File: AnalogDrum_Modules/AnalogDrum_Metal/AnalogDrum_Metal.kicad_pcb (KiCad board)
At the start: 2 copper layers, 100.3 x 160 mm, 177 parts, among them J101 Conn_01x05_Male, Q201 2N3904, Q202 2N3904, Q203 2N3904, Q501 2N3906, Q502 2N3906, Q503 2N3906, Q504 2N3904, Q505 2N3904, Q506 2N3904, Q701 2N3904, Q702 2N3904, Q703 2N3904, SW601 SW_DPDT_x2, SW602 SW_DPDT_x2, U201 TL074, U202 LM358, U301 NE5532, U401 NE5532, U402 LM13700, U403 NE5532, U501 NE5532, U502 NE5532, U601 TL074, U701 TL074, U702 LM358

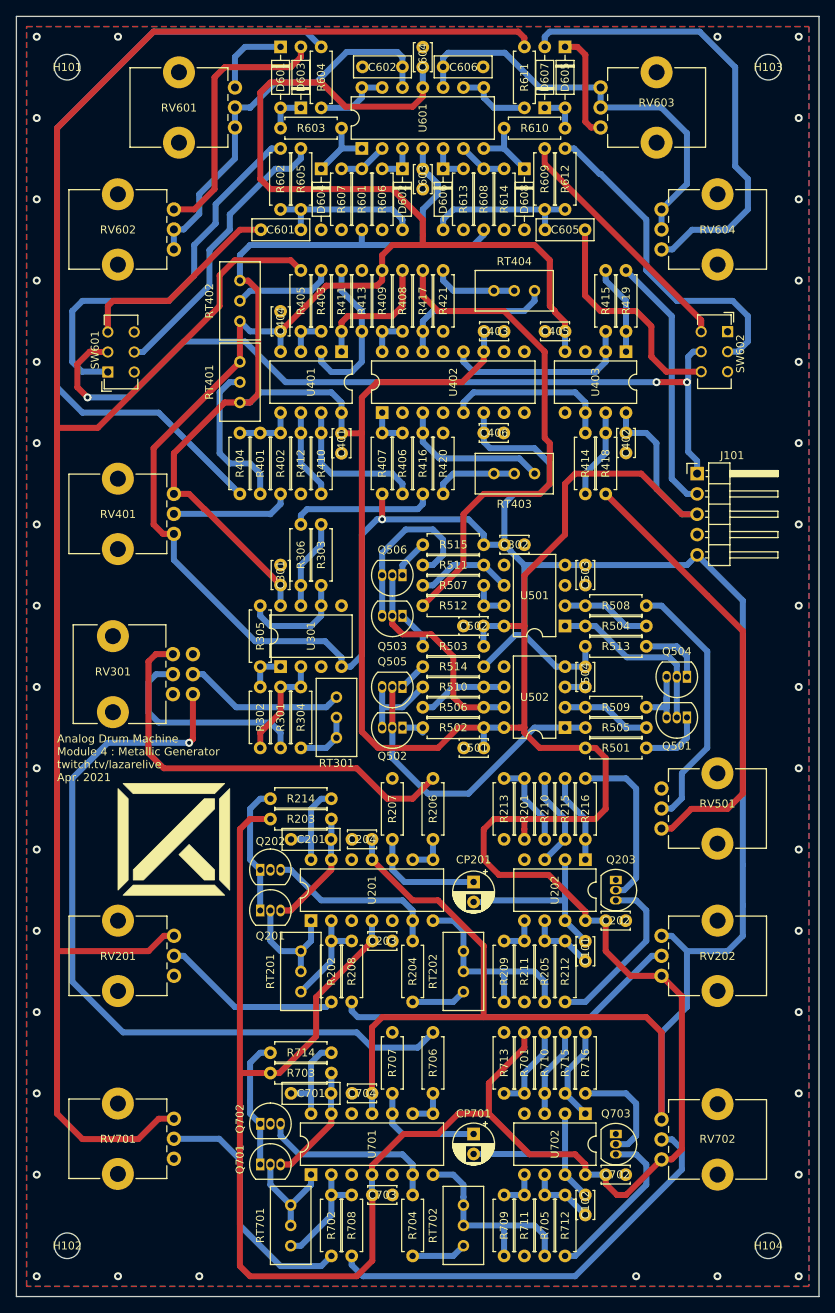
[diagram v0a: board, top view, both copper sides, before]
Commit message: Version 0.1.1
Corrections mineures :
- Vérification des potentiomètres
- Passage des connecteurs de carte e n JST
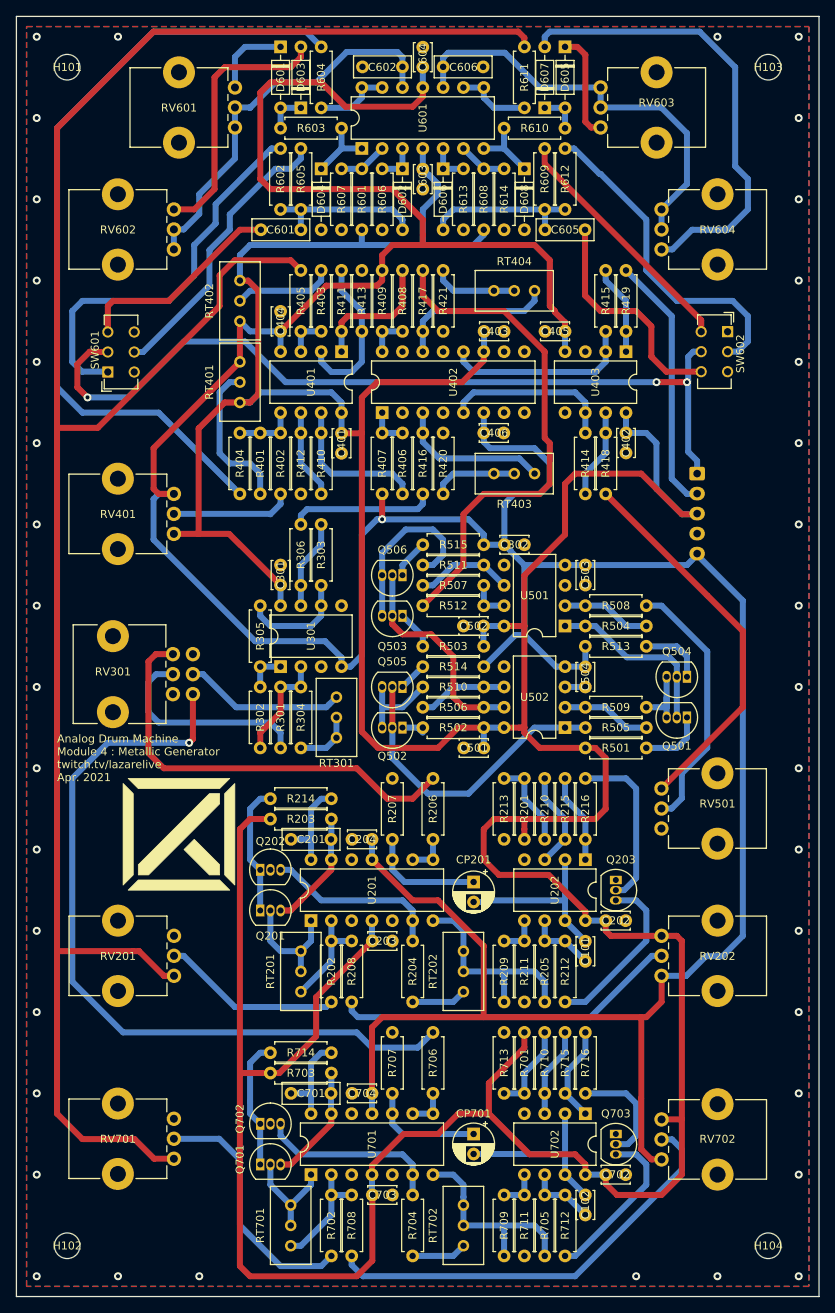
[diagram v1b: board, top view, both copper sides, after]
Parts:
- J101: footprint Connector_PinHeader_2.54mm:PinHeader_1x05_P2.54mm_Horizontal -> Connector_JST:JST_EH_B5B-EH-A_1x05_P2.50mm_Vertical; moved to B.Cu
- moved REF** 0.90 mm to (74.9, 127.6)
- turned J101 to 270 degrees
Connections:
- RV201 pad 1: /EG/EGB_OUT -> GNDA
- RV201 pad 3: GNDA -> /EG/EGB_OUT
- RV202 pad 1: +12V -> -12V
- RV202 pad 3: -12V -> +12V
- RV401 pad 1: +12V -> -12V
- RV401 pad 3: -12V -> +12V
- RV501 pad 1: /WVF/SIGNAL_IN -> GNDA
- RV501 pad 3: GNDA -> /WVF/SIGNAL_IN
- RV701 pad 1: /EG/EGB_OUT -> GNDA
- RV701 pad 3: GNDA -> /EG/EGB_OUT
- RV702 pad 1: +12V -> -12V
- RV702 pad 3: -12V -> +12V
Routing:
- net +12V: track 565.8 -> 574.4 mm
- net /WVF/SIGNAL_IN: track 56.5 -> 48.2 mm
- net -12V: track 482.8 -> 476.4 mm
